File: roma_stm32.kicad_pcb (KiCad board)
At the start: 4 copper layers, 62.5 x 72 mm, 38 parts, among them J1 CAN, J2 Power, J3 Debug_Port, J4 GPIO, J5 IO_I2C, J6 IO_SPI, J7 IO_UART, SW1 SW_RST, U1 TJA1051T-3, U2 STM32L432KBU6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

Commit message: Fix PCB
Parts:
- removed TP4, TP5: TestPoint, TestPoint:TestPoint_Pad_D1.0mm
- C10, C8: footprint Capacitor_SMD:C_1206_3216Metric -> Capacitor_SMD:C_0603_1608Metric
- C9: footprint Capacitor_SMD:C_0805_2012Metric -> Capacitor_SMD:C_0603_1608Metric
- J1: footprint TerminalBlock_Altech:Altech_AK100_1x02_P5.00mm -> TerminalBlock_Phoenix:TerminalBlock_Phoenix_PT-1,5-2-5.0-H_1x02_P5.00mm_Horizontal
- J2: footprint TerminalBlock_Altech:Altech_AK100_1x03_P5.00mm -> TerminalBlock_Phoenix:TerminalBlock_Phoenix_PT-1,5-3-5.0-H_1x03_P5.00mm_Horizontal
- J3: footprint TerminalBlock_Altech:Altech_AK100_1x06_P5.00mm -> TerminalBlock_Phoenix:TerminalBlock_Phoenix_PT-1,5-6-5.0-H_1x06_P5.00mm_Horizontal
- J4: footprint TerminalBlock_Altech:Altech_AK100_1x10_P5.00mm -> TerminalBlock_Phoenix:TerminalBlock_Phoenix_PT-1,5-10-5.0-H_1x10_P5.00mm_Horizontal
- J5: value IO_I2C -> I2C; footprint TerminalBlock_Altech:Altech_AK100_1x04_P5.00mm -> TerminalBlock_Phoenix:TerminalBlock_Phoenix_PT-1,5-4-5.0-H_1x04_P5.00mm_Horizontal
- J6: value IO_SPI -> SPI; footprint TerminalBlock_Altech:Altech_AK100_1x06_P5.00mm -> TerminalBlock_Phoenix:TerminalBlock_Phoenix_PT-1,5-6-5.0-H_1x06_P5.00mm_Horizontal
- J7: value IO_UART -> UART; footprint TerminalBlock_Altech:Altech_AK100_1x04_P5.00mm -> TerminalBlock_Phoenix:TerminalBlock_Phoenix_PT-1,5-4-5.0-H_1x04_P5.00mm_Horizontal
- JP1: value CAN_Resistor -> SolderJumper_2_Open
- R1: value 3.3K -> 120R
- U2: value STM32L432KBU6 -> STM32L432KBUx
- moved J3 25.5 mm to (199.5, 46.5), turned to 180 degrees
- moved J5 15.5 mm to (166.0, 44.0), turned to -90 degrees
- moved J2 10.0 mm to (166.0, 78.0), turned to -90 degrees
- moved J1 4.88 mm to (166.0, 66.1), turned to -90 degrees
- moved JP1 3.60 mm to (172.0, 70.1), turned to 90 degrees
- moved R2 3.45 mm to (172.0, 66.5)
- moved C8 0.80 mm to (187.2, 79.0)
- moved C10 0.73 mm to (173.2, 79.0)
- turned C6 to 180 degrees
- turned C7 to -90 degrees
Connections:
- C6 pad 1: Net-(U2-NRST) -> GND
- C6 pad 2: GND -> Net-(U2-NRST)
- C7 pad 1: +3V3 -> GND
- C7 pad 2: GND -> +3V3
- J1 pad 1: CAN- -> CAN_H
- J1 pad 2: CAN+ -> CAN_L
- J2 pad 1: GND -> +12V
- J2 pad 3: +12V -> GND
- J3 pad 2: Debug_UART_RX -> JTAG_SWDIO
- J3 pad 3: Debug_UART_TX -> JTAG_SWCLK
- J3 pad 4: JTAG_SWCLK -> Debug_UART_TX
- J3 pad 5: JTAG_SWDIO -> Debug_UART_RX
- J5 pad 2: IO_I2C_SDA -> IO_I2C_SCL
- J5 pad 3: IO_I2C_SCL -> IO_I2C_SDA
- JP1 pad 1: CAN+ -> CAN_L
- R2 pad 1: Net-(JP1-B) -> CAN_H
- R2 pad 2: CAN- -> Net-(JP1-B)
- U1 pad 6: CAN- -> CAN_L
- U1 pad 7: CAN+ -> CAN_H
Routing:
- net CAN_H: track 0.00 -> 15.6 mm
- net CAN+: track 15.6 -> 0.00 mm
- net CAN_L: track 0.00 -> 13.1 mm
- net CAN-: track 13.1 -> 0.00 mm
- net GND: track 55.1 -> 56.6 mm
- net +12V: track 43.1 -> 44.6 mm
- net LED: track 17.7 -> 16.8 mm
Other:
- board size 62.5 x 72 mm -> 65 x 72.5 mm

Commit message: WIP: Prepare for JLC
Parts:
- removed C6: 10uF, Capacitor_SMD:C_0603_1608Metric
- added R5: 1K8, Resistor_SMD:R_0603_1608Metric, F.Cu at (198.3, 64.5)
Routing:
- net GND: track 56.6 -> 52.3 mm
- net +3V3: track 34.1 -> 36.9 mm
- net Net-(U2-NRST): track 15.0 -> 14.4 mm

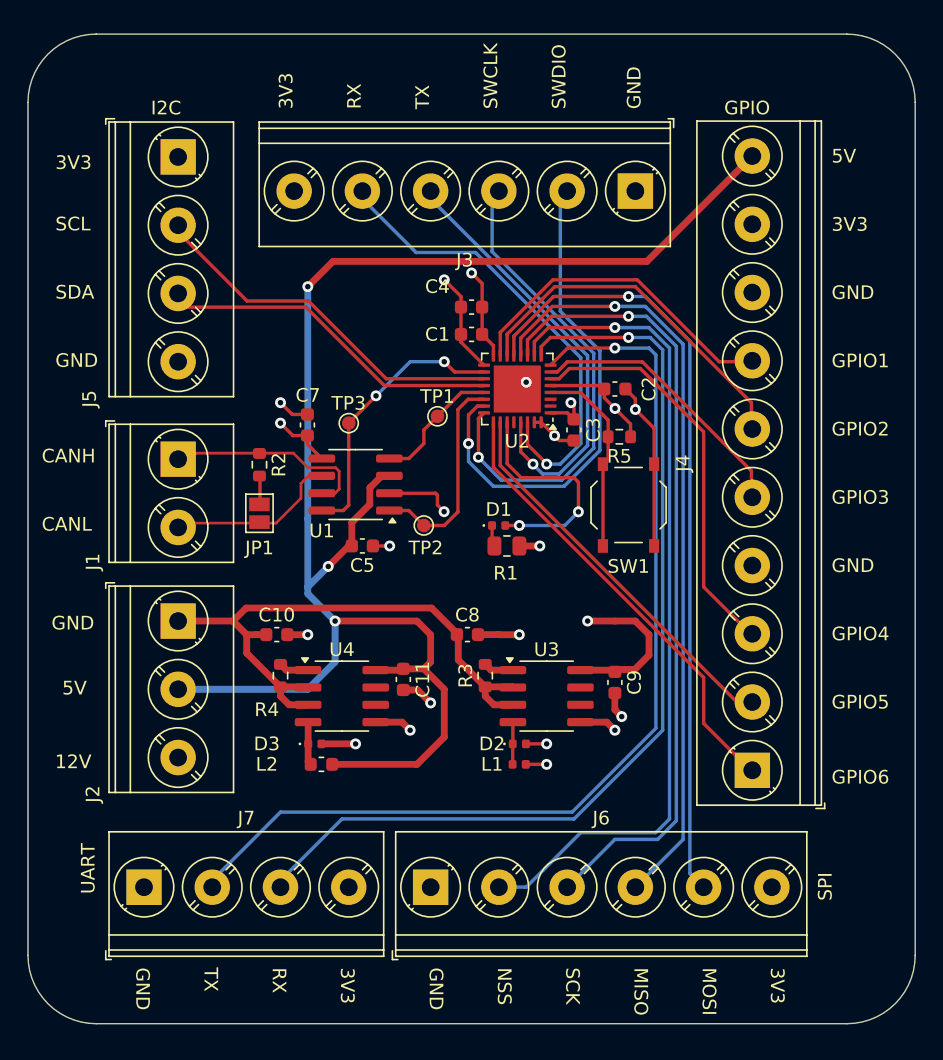
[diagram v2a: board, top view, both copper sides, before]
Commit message: Replace power regulators; Pick all JLC components
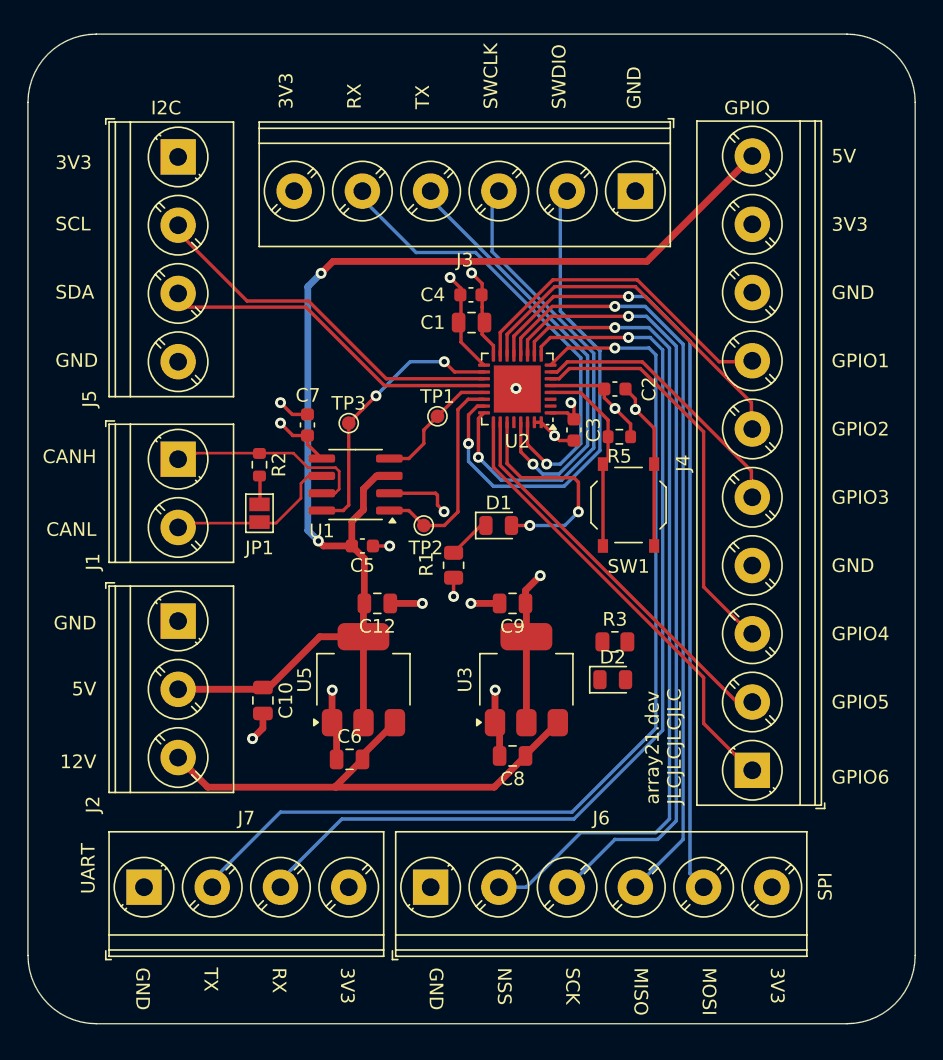
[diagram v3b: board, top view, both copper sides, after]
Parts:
- removed C11: 330uF, Capacitor_SMD:C_0603_1608Metric
- removed D3: D_Schottky, Diode_SMD:D_0402_1005Metric
- removed L1: 1uH, Inductor_SMD:L_0402_1005Metric
- removed L2: 330u, Inductor_SMD:L_0603_1608Metric
- removed R4: 220R, Resistor_SMD:R_0603_1608Metric
- removed U4: ADP1108AR-5, Package_SO:SOIC-8_3.9x4.9mm_P1.27mm
- added C12: 10uF, Capacitor_SMD:C_0805_2012Metric, F.Cu at (180.6, 76.7)
- added C6: 10uF, Capacitor_SMD:C_0805_2012Metric, F.Cu at (178.6, 88.1)
- added U5: AMS1117-5.0, Package_TO_SOT_SMD:SOT-223-3_TabPin2, F.Cu at (179.6, 82.3)
- C1: footprint Capacitor_SMD:C_0603_1608Metric -> Capacitor_SMD:C_0805_2012Metric
- C10, C8: value 100uF -> 10uF; footprint Capacitor_SMD:C_0603_1608Metric -> Capacitor_SMD:C_0805_2012Metric
- C9: value 330uF -> 10uF; footprint Capacitor_SMD:C_0603_1608Metric -> Capacitor_SMD:C_0805_2012Metric
- D1: value LED -> DBG_LED; footprint LED_SMD:LED_0402_1005Metric -> LED_SMD:LED_0805_2012Metric
- D2: value D_Schottky -> PWR_LED; footprint Diode_SMD:D_0402_1005Metric -> LED_SMD:LED_0805_2012Metric
- R3: value 100R -> 120R; footprint Resistor_SMD:R_0603_1608Metric -> Resistor_SMD:R_0805_2012Metric
- U3: value ADP1108AR-3.3 -> AMS1117-3.3; footprint Package_SO:SOIC-8_3.9x4.9mm_P1.27mm -> Package_TO_SOT_SMD:SOT-223-3_TabPin2
- moved R3 9.82 mm to (198.0, 79.5), turned to 0 degrees
- moved C8 9.48 mm to (190.5, 87.9), turned to 180 degrees
- moved C9 9.48 mm to (190.5, 76.7), turned to 180 degrees
- moved D2 8.30 mm to (197.8, 82.3)
- moved C10 4.93 mm to (172.2, 83.8), turned to -90 degrees
- moved R1 4.15 mm to (186.2, 73.9), turned to -90 degrees
- moved U3 1.91 mm to (191.5, 82.3), turned to 90 degrees
- moved C4 0.90 mm to (187.5, 54.1)
- moved C1 0.87 mm to (187.5, 56.1)
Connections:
- C10 pad 1: +12V -> +5V
- D2 pad 2: GND -> +12V
- J2 pad 1: +12V -> GND
- J2 pad 3: GND -> +12V
- R3 pad 1: +12V -> Net-(D2-K)
- R3 pad 2: Net-(U3-Ilim) -> GND
- U3 pad 1: Net-(U3-Ilim) -> GND
- U3 pad 2: +12V -> +3V3
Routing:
- net +5V: track 117.0 -> 93.3 mm, vias 3 -> 2
- net +12V: track 44.6 -> 37.2 mm
- net Net-(D3-K): track 3.17 -> 0.00 mm
- net Net-(D2-K): track 3.11 -> 0.00 mm
- net GND: track 52.3 -> 49.9 mm, vias 16 -> 13
- net Net-(U4-Ilim): track 2.20 -> 0.00 mm
- net Net-(U3-Ilim): track 2.20 -> 0.00 mm
- net +3V3: track 36.9 -> 34.7 mm, vias 6 -> 5
- net Net-(D1-K): track 1.57 -> 3.34 mm
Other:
- board text added: "array21.dev JLCJLCJLCJLC"

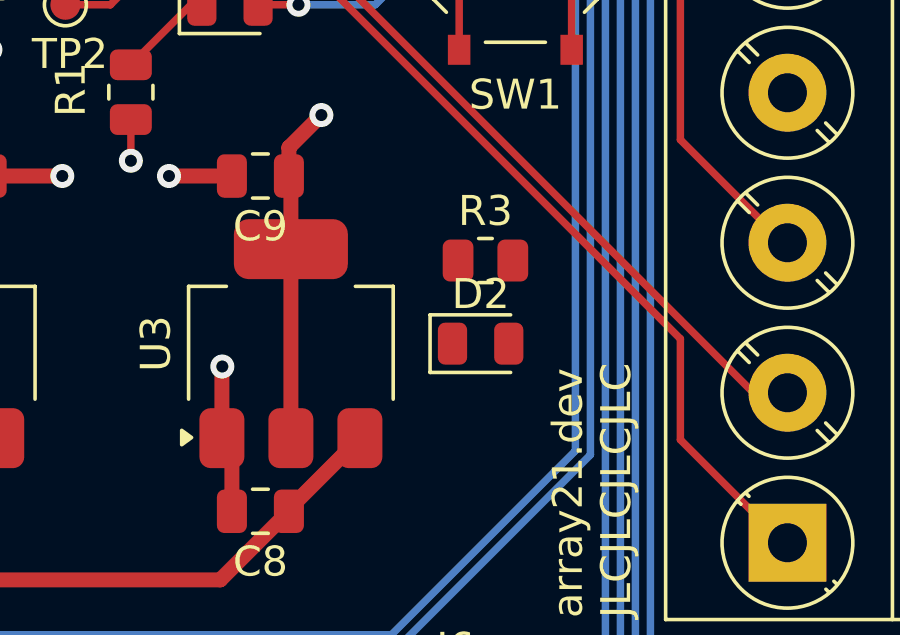
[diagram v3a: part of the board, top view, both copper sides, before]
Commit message: Attach power LED
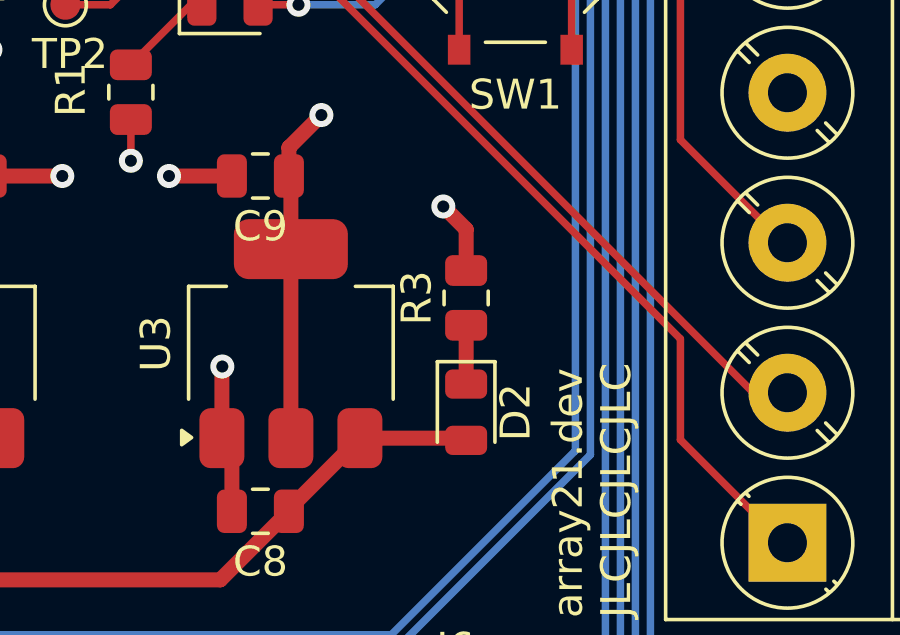
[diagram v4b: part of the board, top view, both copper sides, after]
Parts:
- moved D2 2.34 mm to (197.4, 84.6), turned to -90 degrees
- moved R3 1.40 mm to (197.4, 80.8), turned to 90 degrees
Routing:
- net +12V: track 37.2 -> 40.8 mm
- net GND: track 49.9 -> 52.4 mm, vias 13 -> 14
- net Net-(D2-K): track 0.00 -> 1.96 mm
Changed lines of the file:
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@@
 	(footprint "Resistor_SMD:R_0805_2012Metric"
 		(layer "F.Cu")
-		(at 198.0005 79.526)
+		(at 197.358 80.772 90)
 		(descr "Resistor SMD 0805 (2012 Metric), square (rectangular) end terminal, IPC_7351 nominal, (Body size source: IPC-SM-782 page 72, https://www.pcb-3d.com/wordpress/wp-content/uploads/ipc-sm-782a_amendment_1_and_2.pdf), generated with kicad-footprint-generator")
 		(tags "resistor")
 		(property "Reference" "R3"
-			(at 0 -1.65 0)
+			(at 0 -1.65 90)
 			(layer "F.SilkS")
 			(effects
@@
 		)
 		(property "Value" "120R"
-			(at 0 1.65 0)
+			(at 0 1.65 90)
 			(layer "F.Fab")
 			(effects
@@
 		)
 		(property "Footprint" "Resistor_SMD:R_0805_2012Metric"
-			(at 0 0 0)
+			(at 0 0 90)
 			(layer "F.Fab")
 			(hide yes)
@@
 		)
 		(property "Datasheet" ""
-			(at 0 0 0)
+			(at 0 0 90)
 			(layer "F.Fab")
 			(hide yes)
@@
 		)
 		(property "Description" "Resistor"
-			(at 0 0 0)
+			(at 0 0 90)
 			(layer "F.Fab")
 			(hide yes)
@@
 		)
 		(property "LCSC" "C17437"
-			(at 0 0 0)
+			(at 0 0 90)
 			(layer "F.SilkS")
 			(hide yes)
@@
 		)
 		(fp_line
-			(start -1.68 -0.95)
-			(end 1.68 -0.95)
+			(start 1.68 -0.95)
+			(end 1.68 0.95)
 			(stroke
 				(width 0.05)
@@
 		)
 		(fp_line
-			(start -1.68 0.95)
-			(end -1.68 -0.95)
+			(start -1.68 -0.95)
+			(end 1.68 -0.95)
 			(stroke
 				(width 0.05)
@@
 		)
 		(fp_line
-			(start 1.68 -0.95)
-			(end 1.68 0.95)
+			(start 1.68 0.95)
+			(end -1.68 0.95)
 			(stroke
 				(width 0.05)
@@
 		)
 		(fp_line
-			(start 1.68 0.95)
-			(end -1.68 0.95)
+			(start -1.68 0.95)
+			(end -1.68 -0.95)
 			(stroke
 				(width 0.05)
@@
 		)
 		(fp_line
-			(start -1 -0.625)
-			(end 1 -0.625)
+			(start 1 -0.625)
+			(end 1 0.625)
 			(stroke
 				(width 0.1)
@@
 		)
 		(fp_line
-			(start -1 0.625)
-			(end -1 -0.625)
+			(start -1 -0.625)
+			(end 1 -0.625)
 			(stroke
 				(width 0.1)
@@
 		)
 		(fp_line
-			(start 1 -0.625)
-			(end 1 0.625)
+			(start 1 0.625)
+			(end -1 0.625)
 			(stroke
 				(width 0.1)
@@
 		)
 		(fp_line
-			(start 1 0.625)
-			(end -1 0.625)
+			(start -1 0.625)
+			(end -1 -0.625)
 			(stroke
 				(width 0.1)
@@
 		)
 		(fp_text user "${REFERENCE}"
-			(at 0 0 0)
+			(at 0 0 90)
 			(layer "F.Fab")
 			(effects
@@
 		)
 		(pad "1" smd roundrect
-			(at -0.9125 0)
+			(at -0.9125 0 90)
 			(size 1.025 1.4)
 			(layers "F.Cu" "F.Paste" "F.Mask")
@@
 		)
 		(pad "2" smd roundrect
-			(at 0.9125 0)
+			(at 0.9125 0 90)
 			(size 1.025 1.4)
 			(layers "F.Cu" "F.Paste" "F.Mask")
@@
 	(footprint "LED_SMD:LED_0805_2012Metric"
 		(layer "F.Cu")
-		(at 197.8405 82.296)
+		(at 197.358 84.582 -90)
 		(descr "LED SMD 0805 (2012 Metric), square (rectangular) end terminal, IPC_7351 nominal, (Body size source: https://docs.google.com/spreadsheets/d/1BsfQQcO9C6DZCsRaXUlFlo91Tg2WpOkGARC1WS5S8t0/edit?usp=sharing), generated with kicad-footprint-generator")
 		(tags "LED")
 		(property "Reference" "D2"
-			(at 0 -1.65 0)
+			(at 0 -1.65 90)
 			(layer "F.SilkS")
 			(effects
@@
 		)
 		(property "Value" "PWR_LED"
-			(at 0 1.65 0)
+			(at 0 1.65 90)
 			(layer "F.Fab")
 			(effects
@@
 		)
 		(property "Footprint" "LED_SMD:LED_0805_2012Metric"
-			(at 0 0 0)
+			(at 0 0 90)
 			(layer "F.Fab")
 			(hide yes)
@@
 		)
 		(property "Datasheet" ""
-			(at 0 0 0)
+			(at 0 0 90)
 			(layer "F.Fab")
 			(hide yes)
@@
 		)
 		(property "Description" "Light emitting diode"
-			(at 0 0 0)
+			(at 0 0 90)
 			(layer "F.Fab")
 			(hide yes)
@@
 		(attr smd)
 		(fp_line
-			(start -1.685 -0.96)
-			(end -1.685 0.96)
+			(start -1.685 0.96)
+			(end 1 0.96)
 			(stroke
 				(width 0.12)
@@
 		)
 		(fp_line
-			(start -1.685 0.96)
-			(end 1 0.96)
+			(start -1.685 -0.96)
+			(end -1.685 0.96)
 			(stroke
 				(width 0.12)
@@
 		)
 		(fp_line
-			(start -1.68 -0.95)
-			(end 1.68 -0.95)
+			(start -1.68 0.95)
+			(end -1.68 -0.95)
 			(stroke
 				(width 0.05)
@@
 		)
 		(fp_line
-			(start -1.68 0.95)
-			(end -1.68 -0.95)
+			(start 1.68 0.95)
+			(end -1.68 0.95)
 			(stroke
 				(width 0.05)
@@
 		)
 		(fp_line
-			(start 1.68 -0.95)
-			(end 1.68 0.95)
+			(start -1.68 -0.95)
+			(end 1.68 -0.95)
 			(stroke
 				(width 0.05)
@@
 		)
 		(fp_line
-			(start 1.68 0.95)
-			(end -1.68 0.95)
+			(start 1.68 -0.95)
+			(end 1.68 0.95)
 			(stroke
 				(width 0.05)
@@
 		)
 		(fp_line
-			(start -1 -0.3)
-			(end -1 0.6)
+			(start -1 0.6)
+			(end 1 0.6)
 			(stroke
 				(width 0.1)
@@
 		)
 		(fp_line
-			(start -1 0.6)
-			(end 1 0.6)
+			(start 1 0.6)
+			(end 1 -0.6)
 			(stroke
 				(width 0.1)
@@
 		)
 		(fp_line
-			(start -0.7 -0.6)
-			(end -1 -0.3)
+			(start -1 -0.3)
+			(end -1 0.6)
 			(stroke
 				(width 0.1)
@@
 		)
 		(fp_line
-			(start 1 -0.6)
-			(end -0.7 -0.6)
+			(start -0.7 -0.6)
+			(end -1 -0.3)
 			(stroke
 				(width 0.1)
@@
 		)
 		(fp_line
-			(start 1 0.6)
-			(end 1 -0.6)
+			(start 1 -0.6)
+			(end -0.7 -0.6)
 			(stroke
 				(width 0.1)
@@
 		)
 		(fp_text user "${REFERENCE}"
-			(at 0 0 0)
+			(at 0 0 90)
 			(layer "F.Fab")
 			(effects
@@
 		)
 		(pad "1" smd roundrect
-			(at -0.9375 0)
+			(at -0.9375 0 270)
 			(size 0.975 1.4)
 			(layers "F.Cu" "F.Paste" "F.Mask")
@@
 		)
 		(pad "2" smd roundrect
-			(at 0.9375 0)
+			(at 0.9375 0 270)
 			(size 0.975 1.4)
 			(layers "F.Cu" "F.Paste" "F.Mask")
@@
 	)
 	(segment
+		(start 197.358 79.8595)
+		(end 197.358 78.486)
+		(width 0.5)
+		(layer "F.Cu")
+		(net 2)
+	)
+	(segment
 		(start 192.1 63.4375)
 		(end 192.6 63.4375)
@@
 	)
 	(segment
+		(start 197.358 78.486)
+		(end 196.596 77.724)
+		(width 0.5)
+		(layer "F.Cu")
+		(net 2)
+	)
+	(segment
 		(start 189.1 57.825)
 		(end 188.275 57)
@@
 	)
 	(via
+		(at 196.596 77.724)
+		(size 0.8)
+		(drill 0.4)
+		(layers "F.Cu" "B.Cu")
+		(net 2)
+	)
+	(via
 		(at 187.5 52.5)
 		(size 0.8)
@@
 	)
 	(segment
+		(start 197.2845 85.446)
+		(end 197.358 85.5195)
+		(width 0.5)
+		(layer "F.Cu")
+		(net 5)
+	)
+	(segment
+		(start 193.816 85.446)
+		(end 197.2845 85.446)
+		(width 0.5)
+		(layer "F.Cu")
+		(net 5)
+	)
+	(segment
 		(start 191.45 87.812)
 		(end 193.816 85.446)
@@
 	)
 	(segment
+		(start 197.358 83.6445)
+		(end 197.358 81.6845)
+		(width 0.5)
+		(layer "F.Cu")
+		(net 32)
+	)
+	(segment
